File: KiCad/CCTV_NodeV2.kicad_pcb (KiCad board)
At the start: 2 copper layers, 95 x 95 mm, 13 parts, among them J1 Solar 6V/10W, J2 Battery (ext, 2× 18650 ||), U1 CN3791, U2 TC4056A_BMS, U3 MT3608, U4 ESP32-S3-DevKitC-1 N16R8, U5 OV7670

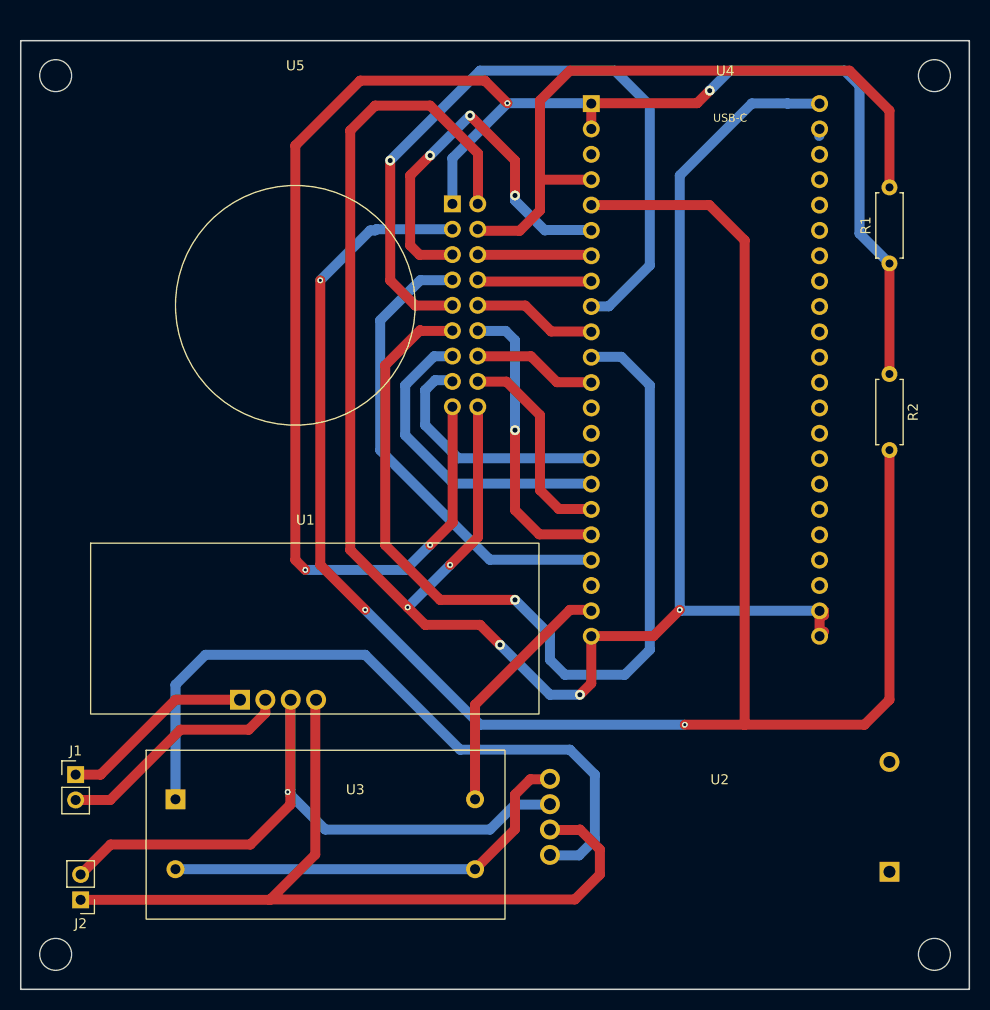
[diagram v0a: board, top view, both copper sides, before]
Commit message: KiCad: clean up U5 (OV7670) symbol/footprint + convert U4 to 40-pin
U5 OV7670 symbol: redrawn to match the module silkscreen (pins renamed
3.3V/SCL/VS/PLK/D7.../DGND/SDA/HS/XLK..., then re-laid into a single
left-hand column in connector order 1-18). Power-symbol net-name text
repositioned so it no longer overlaps the signal labels.

U5 footprint on PCB: moved the 2x9 header to the left of the lens (matching
the photo) by translating the pads -34mm; old/dangling routing ripped up
(U5 now unrouted, ratsnest ready to re-route). Pin numbering/nets unchanged.

U4 ESP32-S3: converted the 44-pin (2x22) symbol to a clean 40-pin (2x20).
Dropped the 4 padless duplicate power pins (2/22/23/44) and renumbered the
remaining pins/pads 1-40 consistently across symbol, footprint and PCB so
each physical pad keeps its net.

Verified: ERC 0, netlists preserved, PCB DRC clean apart from the expected
U5-unrouted ratsnest and the U5 instance-vs-library footprint note.

Co-Authored-By: Claude Opus 4.8 <noreply@anthropic.com>
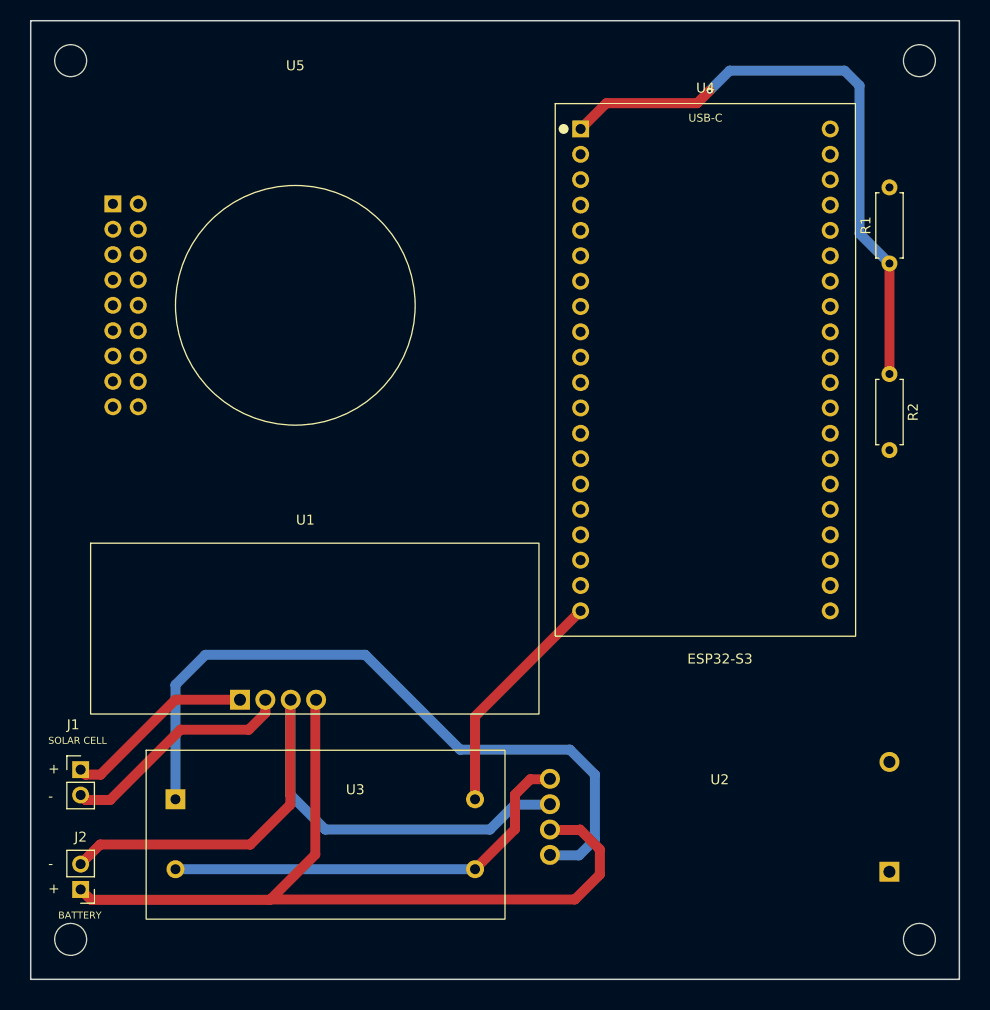
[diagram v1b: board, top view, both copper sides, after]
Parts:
- removed ? (x4): , MountingHole:MountingHole_3.2mm
- U4: value ESP32-S3-DevKitC-1 N16R8 -> ESP32-S3-WROOM-1 N16R8 CAM; footprint CCTV_RPi4:ESP32-S3-DevKitC-1 -> CCTV_RPi4:ESP32-S3-CAM-N16R8_2x20_P2.54mm
- moved J2 1.04 mm to (22.0, 117.0)
- moved J1 0.71 mm to (22.0, 105.0)
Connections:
- U4 pad 10: /CAM_D6 -> /CAM_D5
- U4 pad 11: /CAM_D5 -> /CAM_D2
- U4 pad 12: /CAM_D2 -> unconnected-(U4-GPIO3-Pad13)
- U4 pad 14: unconnected-(U4-GPIO46-Pad14) (its old number) -> /CAM_D1
- U4 pad 15: /CAM_D1 -> /CAM_D3
- U4 pad 16: /CAM_D3 -> /CAM_D0
- U4 pad 17: /CAM_D0 -> /CAM_D4
- U4 pad 18: /CAM_D4 -> /PCLK
- U4 pad 19: /PCLK -> unconnected-(U4-GPIO14-Pad20)
- U4 pad 2: +3V3 -> unconnected-(U4-RST-Pad3)
- U4 pad 20: unconnected-(U4-GPIO14-Pad20) -> +5V
- U4 pad 21: +5V -> unconnected-(U4-GPIO43-Pad24)
- U4 pad 22: GND -> unconnected-(U4-GPIO44-Pad25)
- U4 pad 23: GND -> unconnected-(U4-GPIO1-Pad26)
- U4 pad 3: unconnected-(U4-RST-Pad3) -> /SIOD
- U4 pad 4: /SIOD -> /SIOC
- U4 pad 40: unconnected-(U4-GPIO21-Pad40) (its old number) -> GND
- U4 pad 5: /SIOC -> /VSYNC
- U4 pad 6: /VSYNC -> /HREF
- U4 pad 7: /HREF -> /XCLK
- U4 pad 8: /XCLK -> /CAM_D7
- U4 pad 9: /CAM_D7 -> /CAM_D6
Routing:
- net GND: track 210.4 -> 0.00 mm, vias 5 -> 0
- net /SIOC: track 198.9 -> 0.00 mm, vias 3 -> 0
- net +3V3: track 178.5 -> 61.1 mm, vias 4 -> 1
- net /CAM_D5: track 93.7 -> 0.00 mm, vias 1 -> 0
- net /CAM_D7: track 73.6 -> 0.00 mm, vias 1 -> 0
- net /SIOD: track 68.6 -> 0.00 mm
- net /PCLK: track 47.5 -> 0.00 mm
- net /VSYNC: track 39.3 -> 0.00 mm, vias 3 -> 0
- net /CAM_D3: track 31.5 -> 0.00 mm
- net /CAM_D4: track 29.6 -> 0.00 mm, vias 1 -> 0
- net /CAM_D1: track 24.6 -> 0.00 mm
- net /CAM_D0: track 20.9 -> 0.00 mm
- net /CAM_D2: track 12.3 -> 0.00 mm
- net /CAM_D6: track 12.3 -> 0.00 mm
- net /HREF: track 11.2 -> 0.00 mm
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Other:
- board size 95 x 95 mm -> 93 x 96 mm
- board text added: "+"
- board text added: "-"
- board text added: "BATTERY"
- board text added: "ESP32-S3"
- board text added: "SOLAR CELL"
